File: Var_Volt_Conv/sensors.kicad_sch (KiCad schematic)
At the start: 6 parts, among them U401 INA215BIDCKR, U402 INA215BIDCKR

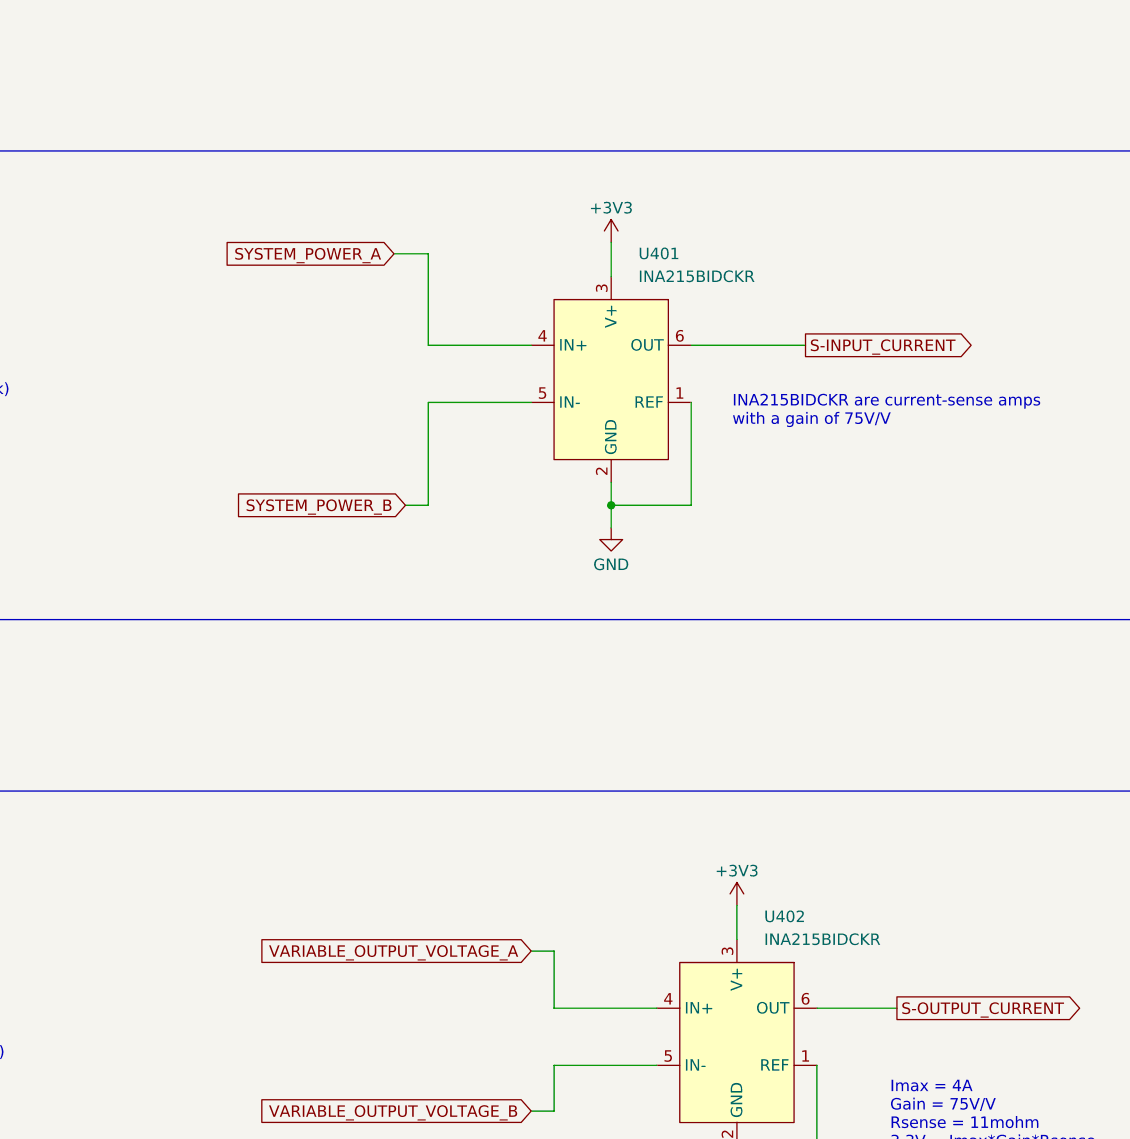
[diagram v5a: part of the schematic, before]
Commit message: Add filter caps to current sensors
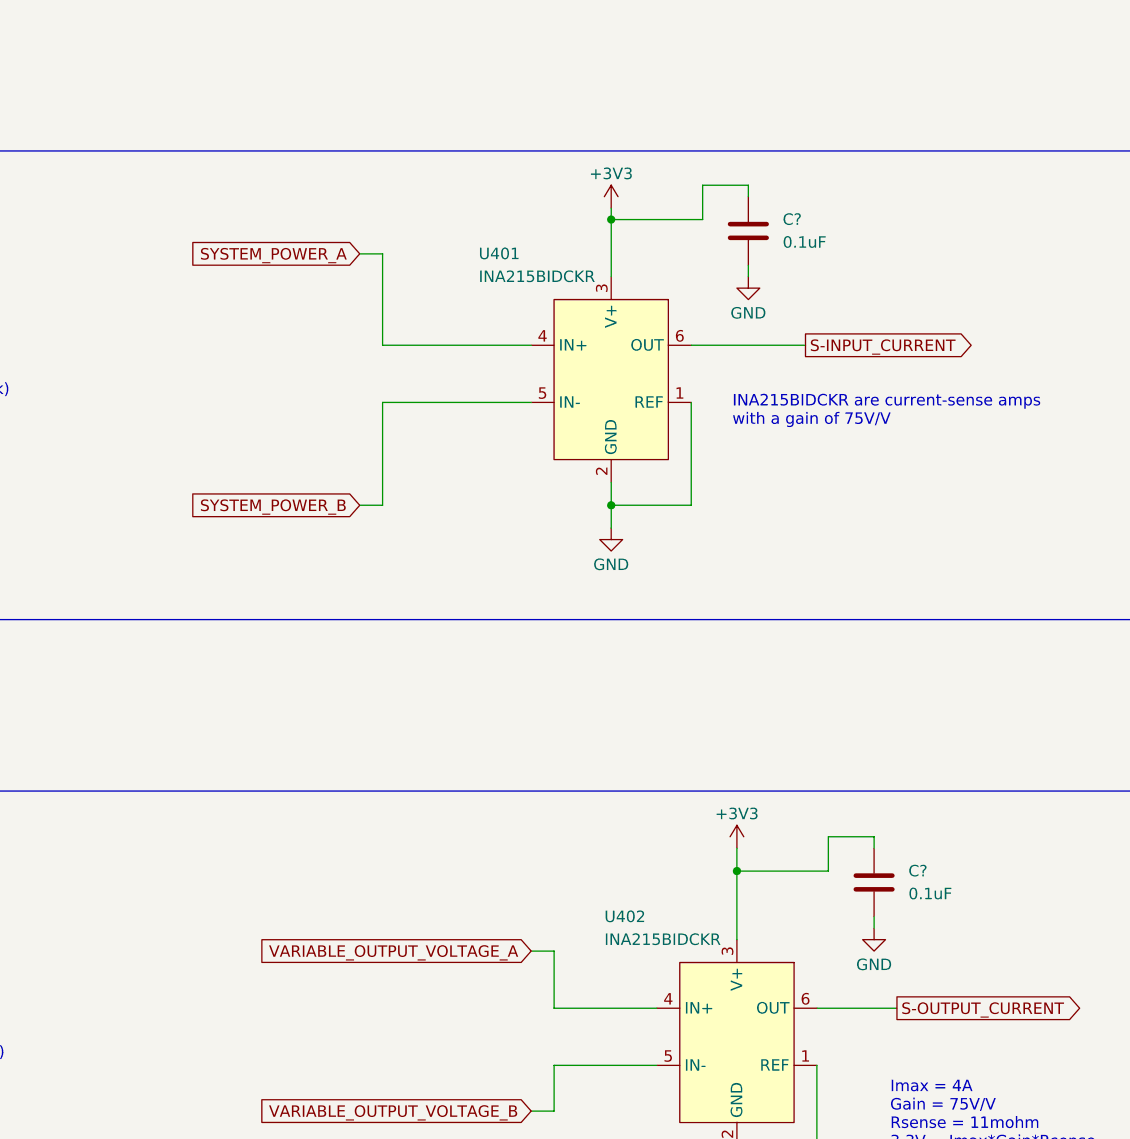
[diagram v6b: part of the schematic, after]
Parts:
- added C? (x2): 0.1uF, symbol Device:C
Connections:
- net +3V3: now also C?.1, C?.1
- net GND: now also C?.2, C?.2

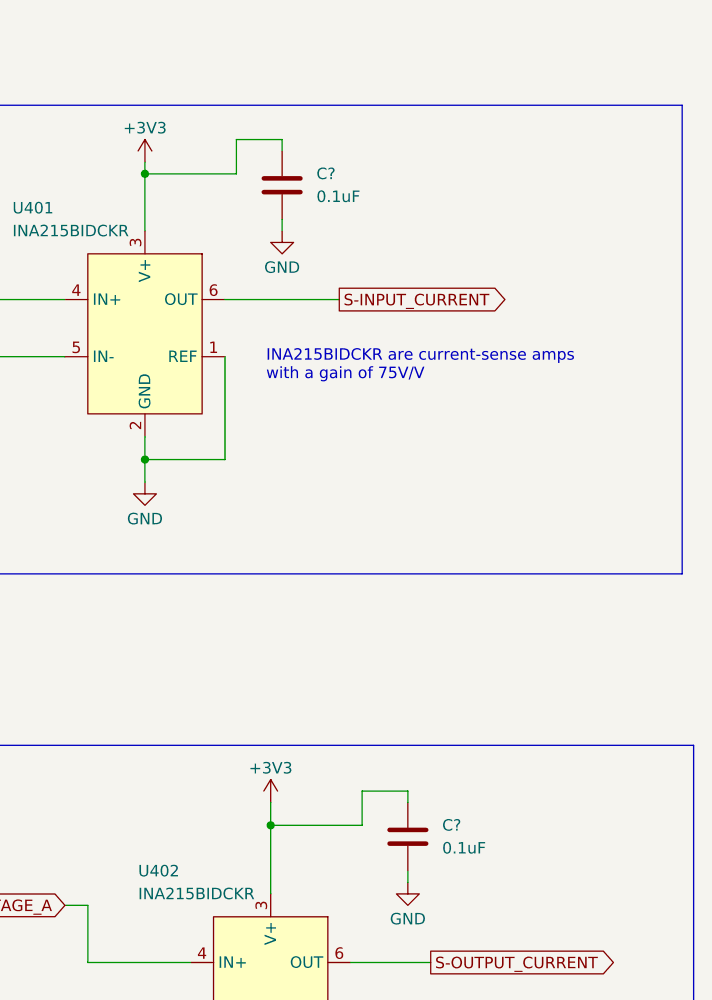
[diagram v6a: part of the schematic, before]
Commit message: Add footprints for all capacitors, and record cap part names
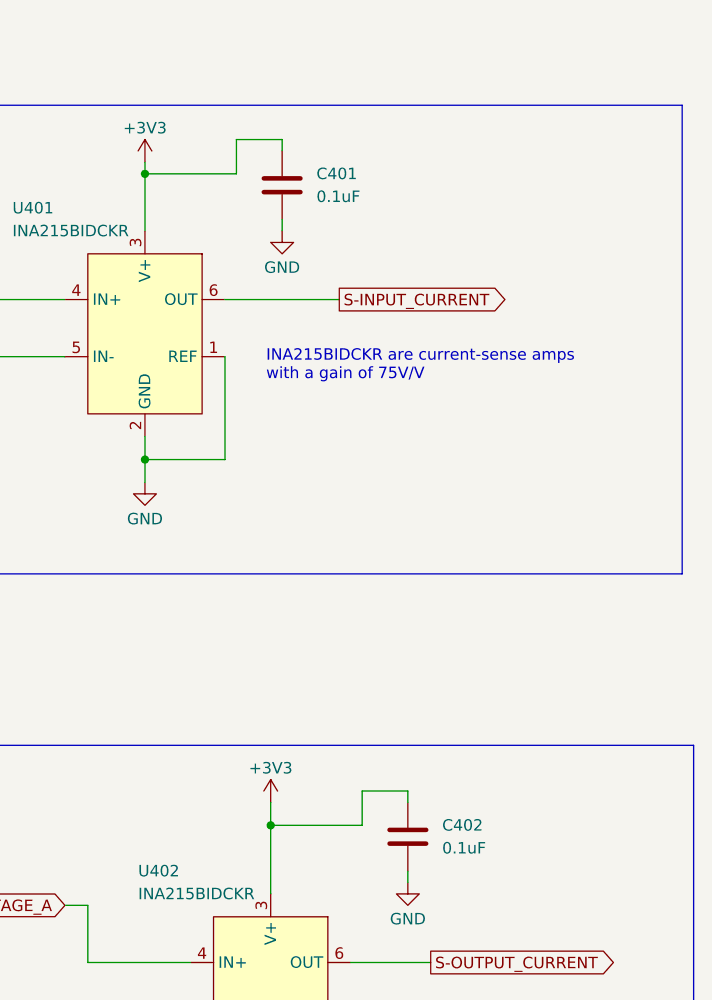
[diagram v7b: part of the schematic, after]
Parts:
- C401, C402: renamed from C?; footprint (none) -> Capacitor_SMD:C_0402_1005Metric
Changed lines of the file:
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@@
 		(dnp no)
 		(fields_autoplaced yes)
-		(property "Reference" "C?"
+		(property "Reference" "C401"
 			(at 208.28 46.9899 0)
 			(effects
@@
 			)
 		)
-		(property "Footprint" ""
+		(property "Footprint" "Capacitor_SMD:C_0402_1005Metric"
 			(at 205.4352 52.07 0)
 			(effects
@@
 			(project ""
 				(path "/7c9580d6-c22f-4506-b9c3-9272e882c9fb/a939aa62-b331-46a3-b3e0-48fa29856a0e"
-					(reference "C?")
+					(reference "C401")
 					(unit 1)
 				)
@@
 		(on_board yes)
 		(dnp no)
-		(property "Reference" "#PWR051"
+		(property "Reference" "#PWR0407"
 			(at 87.63 158.75 0)
 			(effects
@@
 			(project "Var_Volt_Conv"
 				(path "/7c9580d6-c22f-4506-b9c3-9272e882c9fb/a939aa62-b331-46a3-b3e0-48fa29856a0e"
-					(reference "#PWR051")
+					(reference "#PWR0407")
 					(unit 1)
 				)
@@
 		(on_board yes)
 		(dnp no)
-		(property "Reference" "#PWR055"
+		(property "Reference" "#PWR0408"
 			(at 203.2 161.29 0)
 			(effects
@@
 			(project "Var_Volt_Conv"
 				(path "/7c9580d6-c22f-4506-b9c3-9272e882c9fb/a939aa62-b331-46a3-b3e0-48fa29856a0e"
-					(reference "#PWR055")
+					(reference "#PWR0408")
 					(unit 1)
 				)
@@
 		(on_board yes)
 		(dnp no)
-		(property "Reference" "#PWR054"
+		(property "Reference" "#PWR0401"
 			(at 189.23 49.53 0)
 			(effects
@@
 			(project "Var_Volt_Conv"
 				(path "/7c9580d6-c22f-4506-b9c3-9272e882c9fb/a939aa62-b331-46a3-b3e0-48fa29856a0e"
-					(reference "#PWR054")
+					(reference "#PWR0401")
 					(unit 1)
 				)
@@
 		(dnp no)
 		(fields_autoplaced yes)
-		(property "Reference" "C?"
+		(property "Reference" "C402"
 			(at 222.25 119.3799 0)
 			(effects
@@
 			)
 		)
-		(property "Footprint" ""
+		(property "Footprint" "Capacitor_SMD:C_0402_1005Metric"
 			(at 219.4052 124.46 0)
 			(effects
@@
 			(project "Var_Volt_Conv"
 				(path "/7c9580d6-c22f-4506-b9c3-9272e882c9fb/a939aa62-b331-46a3-b3e0-48fa29856a0e"
-					(reference "C?")
+					(reference "C402")
 					(unit 1)
 				)
@@
 		(on_board yes)
 		(dnp no)
-		(property "Reference" "#PWR0305"
+		(property "Reference" "#PWR0402"
 			(at 204.47 59.69 0)
 			(effects
@@
 			(project "Var_Volt_Conv"
 				(path "/7c9580d6-c22f-4506-b9c3-9272e882c9fb/a939aa62-b331-46a3-b3e0-48fa29856a0e"
-					(reference "#PWR0305")
+					(reference "#PWR0402")
 					(unit 1)
 				)
@@
 		(on_board yes)
 		(dnp no)
-		(property "Reference" "#PWR056"
+		(property "Reference" "#PWR0405"
 			(at 203.2 120.65 0)
 			(effects
@@
 			(project "Var_Volt_Conv"
 				(path "/7c9580d6-c22f-4506-b9c3-9272e882c9fb/a939aa62-b331-46a3-b3e0-48fa29856a0e"
-					(reference "#PWR056")
+					(reference "#PWR0405")
 					(unit 1)
 				)
@@
 		(on_board yes)
 		(dnp no)
-		(property "Reference" "#PWR0306"
+		(property "Reference" "#PWR0406"
 			(at 218.44 132.08 0)
 			(effects
@@
 			(project "Var_Volt_Conv"
 				(path "/7c9580d6-c22f-4506-b9c3-9272e882c9fb/a939aa62-b331-46a3-b3e0-48fa29856a0e"
-					(reference "#PWR0306")
+					(reference "#PWR0406")
 					(unit 1)
 				)
@@
 		(on_board yes)
 		(dnp no)
-		(property "Reference" "#PWR048"
+		(property "Reference" "#PWR0403"
 			(at 88.9 86.36 0)
 			(effects
@@
 			(project "Var_Volt_Conv"
 				(path "/7c9580d6-c22f-4506-b9c3-9272e882c9fb/a939aa62-b331-46a3-b3e0-48fa29856a0e"
-					(reference "#PWR048")
+					(reference "#PWR0403")
 					(unit 1)
 				)
@@
 		(on_board yes)
 		(dnp no)
-		(property "Reference" "#PWR053"
+		(property "Reference" "#PWR0404"
 			(at 189.23 87.63 0)
 			(effects
@@
 			(project "Var_Volt_Conv"
 				(path "/7c9580d6-c22f-4506-b9c3-9272e882c9fb/a939aa62-b331-46a3-b3e0-48fa29856a0e"
-					(reference "#PWR053")
-					(unit 1)
-				)
+					(reference "#PWR0404")
+					(unit 1)
+				)

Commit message: Add footprints to current sense amps
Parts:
- U401, U402: footprint (none) -> Package_TO_SOT_SMD:SOT-363_SC-70-6
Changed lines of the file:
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@@
 			)
 		)
-		(property "Footprint" ""
+		(property "Footprint" "Package_TO_SOT_SMD:SOT-363_SC-70-6"
 			(at 203.2 146.05 0)
 			(effects
@@
 			)
 		)
-		(property "Footprint" ""
+		(property "Footprint" "Package_TO_SOT_SMD:SOT-363_SC-70-6"
 			(at 189.23 72.39 0)
 			(effects
